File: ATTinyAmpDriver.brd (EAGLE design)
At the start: 30 x 15 mm, 31 parts, among them Q1 SI2301CDS, Q2 BC846, U1 SPX5205M5-L-3-3, U2 ATTINY5-TSHR, U3 MCP6L2-X_SN, X1 DIODES, X2 INPUT

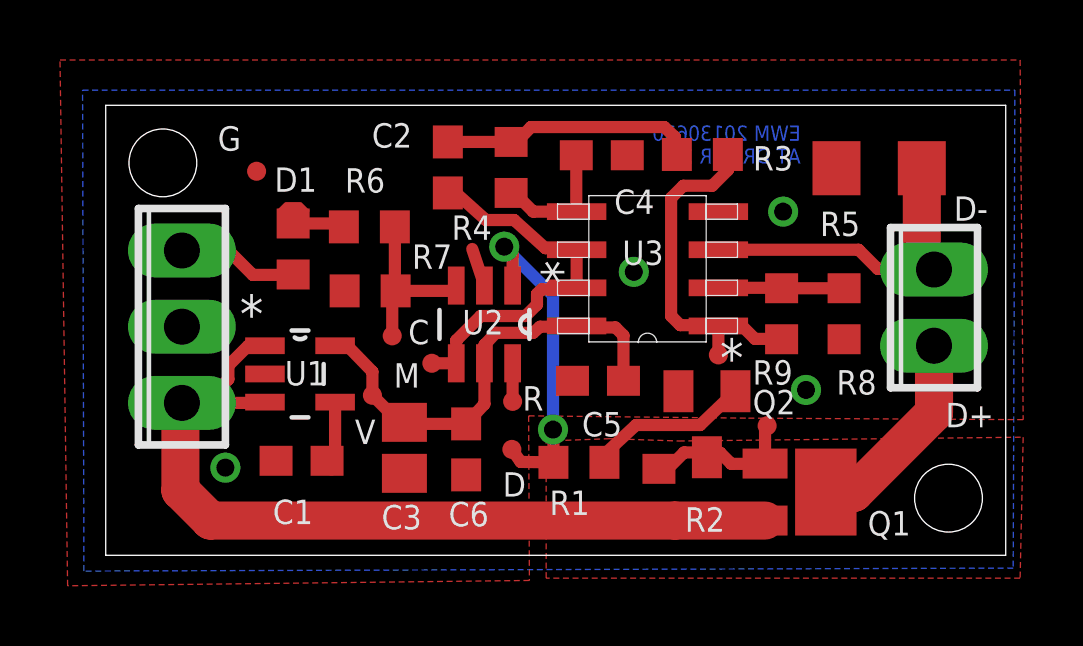
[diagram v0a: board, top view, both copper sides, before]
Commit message: Changed C3 to 1206 47uF
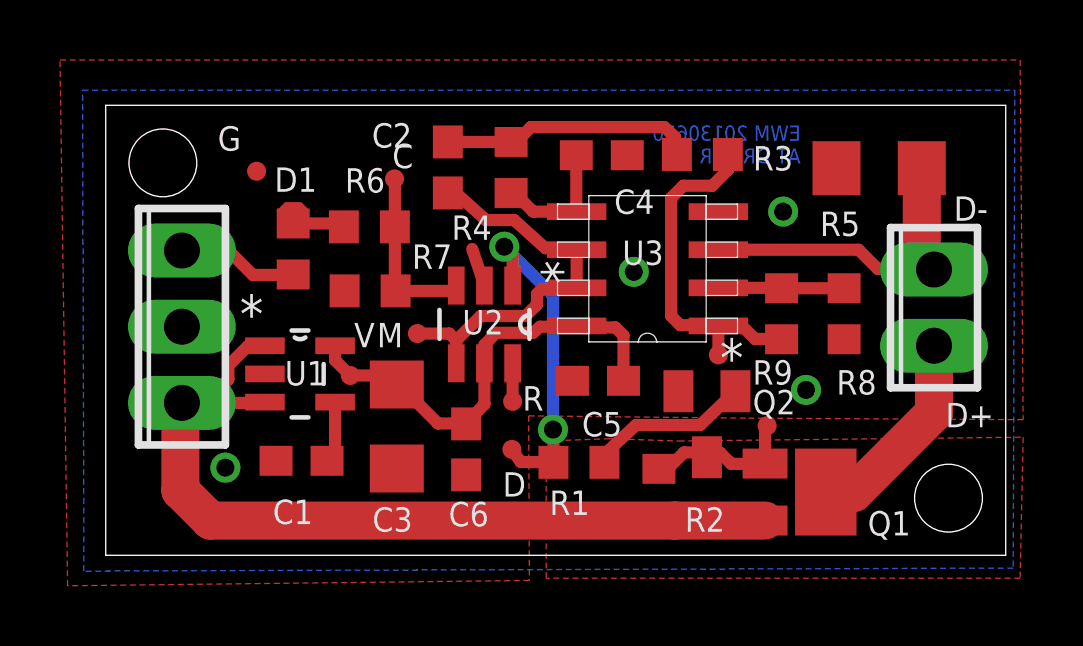
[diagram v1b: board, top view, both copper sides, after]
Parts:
- C3: value 10u -> 47u; device resistor:C0805 -> resistor:C1206
- moved TPICLK 5.23 mm to (9.63, 12.5)
- moved MEASURE 1.10 mm to (10.4, 7.39)
- moved +5V 0.99 mm to (8.15, 5.99)
- moved C3 0.76 mm to (9.70, 4.29)
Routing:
- net MEASURE: track 12.8 -> 13.4 mm
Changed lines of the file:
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@@
 AT DRIVER 3</text>
 <text x="13.2334" y="1.9558" size="0.8128" layer="25">D</text>
-<text x="10.0838" y="7.0358" size="0.8128" layer="25">C</text>
+<text x="9.5504" y="12.9032" size="0.8128" layer="25">C</text>
 <text x="3.7338" y="13.4874" size="0.8128" layer="25">G</text>
 <text x="13.8938" y="4.826" size="0.8128" layer="25">R</text>
-<text x="8.3058" y="3.7084" size="0.8128" layer="25">V</text>
+<text x="8.2804" y="6.9342" size="0.8128" layer="25">V</text>
 <dimension x1="0" y1="15" x2="0" y2="0" x3="-1.9812" y3="7.5" textsize="1.778" layer="20" unit="inch" precision="3"/>
 <dimension x1="0" y1="0" x2="30" y2="0" x3="15" y3="-3.5052" textsize="1.778" layer="20" unit="inch" precision="3"/>
-<text x="9.6012" y="5.588" size="0.8128" layer="25">M</text>
+<text x="9.0424" y="6.9342" size="0.8128" layer="25">M</text>
 </plain>
 <attributes>
@@
 <attribute name="VALUE" x="5.588" y="3.556" size="1.27" layer="27" rot="R90"/>
 </element>
-<element name="C3" library="resistor" package="C0805" value="10u" x="9.9568" y="3.5814" smashed="yes" rot="R270">
-<attribute name="NAME" x="9.1948" y="0.8636" size="0.8128" layer="25"/>
-<attribute name="VALUE" x="7.6708" y="4.4704" size="1.27" layer="27" rot="R270"/>
-<attribute name="DIGIKEY" value="445-7534-1-ND" x="9.9568" y="3.5814" size="1.778" layer="27" rot="R270" display="off"/>
-<attribute name="DIGIKEY_COST" value=".10" x="9.9568" y="3.5814" size="1.778" layer="27" rot="R270" display="off"/>
+<element name="C3" library="resistor" package="C1206" value="47u" x="9.7028" y="4.2926" smashed="yes" rot="R270">
+<attribute name="NAME" x="8.89" y="0.7874" size="0.8128" layer="25"/>
+<attribute name="VALUE" x="7.4168" y="5.1816" size="1.27" layer="27" rot="R270"/>
+<attribute name="DIGIKEY" value="399-5508-1-ND" x="9.7028" y="4.2926" size="1.778" layer="27" rot="R270" display="off"/>
+<attribute name="DIGIKEY_COST" value=".67" x="9.7028" y="4.2926" size="1.778" layer="27" rot="R270" display="off"/>
 </element>
 <element name="R5" library="resistor" package="R1206" value=".1" x="25.781" y="12.9032" smashed="yes">
@@
 </element>
 <element name="TPIDATA" library="Personal" package="TPI_PAD" value="TPI" x="13.5382" y="3.5306"/>
-<element name="TPICLK" library="Personal" package="TPI_PAD" value="TPI" x="9.5504" y="7.3152"/>
-<element name="+5V" library="Personal" package="TPI_PAD" value="TPI" x="8.89" y="5.334"/>
+<element name="TPICLK" library="Personal" package="TPI_PAD" value="TPI" x="9.6266" y="12.5476"/>
+<element name="+5V" library="Personal" package="TPI_PAD" value="TPI" x="8.1534" y="5.9944"/>
 <element name="GND" library="Personal" package="TPI_PAD" value="TPI" x="5.0292" y="12.8016"/>
 <element name="C1" library="resistor" package="C0603" value="10n" x="6.5278" y="3.1496" smashed="yes" rot="R180">
@@
 </element>
 <element name="PWM" library="Personal" package="TPI_PAD" value="TPI" x="22.0472" y="4.318"/>
-<element name="MEASURE" library="Personal" package="TPI_PAD" value="TPI" x="10.8712" y="6.4008"/>
+<element name="MEASURE" library="Personal" package="TPI_PAD" value="TPI" x="10.3886" y="7.3914"/>
 <element name="OUTA" library="Personal" package="TPI_PAD" value="TPI" x="20.4216" y="6.6802"/>
 </elements>
@@
 <contactref element="U2" pad="5"/>
 <contactref element="+5V" pad="P$1"/>
-<wire x1="7.6454" y1="6.985" x2="8.0518" y2="6.985" width="0.4064" layer="1"/>
-<wire x1="8.0518" y1="6.985" x2="8.89" y2="6.1214" width="0.4064" layer="1"/>
-<wire x1="8.89" y1="5.334" x2="8.89" y2="6.1214" width="0.4064" layer="1"/>
-<wire x1="8.89" y1="5.334" x2="8.9662" y2="5.2832" width="0.4064" layer="1"/>
-<wire x1="8.9662" y1="5.2832" x2="8.9916" y2="5.2832" width="0.4064" layer="1"/>
-<wire x1="8.9916" y1="5.2832" x2="8.9916" y2="5.2578" width="0.4064" layer="1"/>
-<wire x1="9.9568" y1="4.4314" x2="9.7926" y2="4.4314" width="0.4064" layer="1"/>
-<wire x1="9.7926" y1="4.4314" x2="8.89" y2="5.334" width="0.4064" layer="1"/>
 <contactref element="C6" pad="1"/>
 <contactref element="C5" pad="1"/>
@@
 <wire x1="12.6238" y1="6.4008" x2="12.6238" y2="5.041" width="0.4064" layer="1"/>
 <wire x1="12.6238" y1="5.041" x2="12.0142" y2="4.3806" width="0.4064" layer="1"/>
-<wire x1="12.0142" y1="4.3806" x2="10.0076" y2="4.3806" width="0.4064" layer="1"/>
-<wire x1="10.0076" y1="4.3806" x2="9.9568" y2="4.4314" width="0.4064" layer="1"/>
+<wire x1="7.6454" y1="6.985" x2="7.6454" y2="6.5024" width="0.4064" layer="1"/>
+<wire x1="7.6454" y1="6.5024" x2="8.1534" y2="5.9944" width="0.4064" layer="1"/>
+<wire x1="8.1534" y1="5.9944" x2="9.401" y2="5.9944" width="0.4064" layer="1"/>
+<wire x1="9.401" y1="5.9944" x2="9.7028" y2="5.6926" width="0.4064" layer="1"/>
+<wire x1="9.7028" y1="5.6926" x2="9.776" y2="5.6926" width="0.4064" layer="1"/>
+<wire x1="9.776" y1="5.6926" x2="11.0744" y2="4.3942" width="0.4064" layer="1"/>
+<wire x1="11.0744" y1="4.3942" x2="12.0006" y2="4.3942" width="0.4064" layer="1"/>
+<wire x1="12.0006" y1="4.3942" x2="12.0142" y2="4.3806" width="0.4064" layer="1"/>
 </signal>
 <signal name="D-">
@@
 <wire x1="15.6464" y1="10.2362" x2="15.6972" y2="10.1854" width="0.4064" layer="1"/>
 <contactref element="MEASURE" pad="P$1"/>
-<wire x1="10.8712" y1="6.4008" x2="11.684" y2="6.4008" width="0.4064" layer="1"/>
+<wire x1="10.3886" y1="7.3914" x2="11.4554" y2="7.3914" width="0.4064" layer="1"/>
+<wire x1="11.4554" y1="7.3914" x2="11.684" y2="7.1628" width="0.4064" layer="1"/>
 </signal>
 <signal name="MOSFET">
@@
 <wire x1="9.6384" y1="8.8392" x2="9.6638" y2="8.8138" width="0.4064" layer="1"/>
 <wire x1="11.7094" y1="8.8138" x2="11.684" y2="8.9916" width="0.4064" layer="1"/>
-<wire x1="9.6638" y1="8.8138" x2="9.5504" y2="8.8138" width="0.4064" layer="1"/>
-<wire x1="9.5504" y1="8.8138" x2="9.5504" y2="7.3152" width="0.4064" layer="1"/>
 <wire x1="9.6638" y1="8.8138" x2="11.684" y2="8.8138" width="0.4064" layer="1"/>
 <wire x1="11.684" y1="8.8138" x2="11.684" y2="8.9916" width="0.4064" layer="1"/>
+<wire x1="9.6266" y1="12.5476" x2="9.6384" y2="12.5476" width="0.4064" layer="1"/>
+<wire x1="9.6384" y1="12.5476" x2="9.6384" y2="10.9474" width="0.4064" layer="1"/>
 </signal>
 <signal name="N$3">
@@
 </signal>
 </signals>
-<errors>
-</errors>
 </board>
 </drawing>

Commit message: Created Programming Fixture
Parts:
- +5V, GND, MEASURE, OUTA, PWM, RESET, TPICLK, TPIDATA: device Personal:TPI_PAD -> Combined:TPI_PAD
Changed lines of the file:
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@@
 <grid distance="0.001" unitdist="inch" unit="inch" style="lines" multiple="1" display="no" altdistance="0.025" altunitdist="inch" altunit="inch"/>
 <layers>
-<layer number="1" name="Top" color="4" fill="1" visible="yes" active="yes"/>
-<layer number="16" name="Bottom" color="1" fill="1" visible="yes" active="yes"/>
-<layer number="17" name="Pads" color="2" fill="1" visible="yes" active="yes"/>
-<layer number="18" name="Vias" color="2" fill="1" visible="yes" active="yes"/>
-<layer number="19" name="Unrouted" color="6" fill="1" visible="yes" active="yes"/>
+<layer number="1" name="Top" color="4" fill="1" visible="no" active="yes"/>
+<layer number="16" name="Bottom" color="1" fill="1" visible="no" active="yes"/>
+<layer number="17" name="Pads" color="2" fill="1" visible="no" active="yes"/>
+<layer number="18" name="Vias" color="2" fill="1" visible="no" active="yes"/>
+<layer number="19" name="Unrouted" color="6" fill="1" visible="no" active="yes"/>
 <layer number="20" name="Dimension" color="15" fill="1" visible="yes" active="yes"/>
-<layer number="21" name="tPlace" color="7" fill="1" visible="yes" active="yes"/>
-<layer number="22" name="bPlace" color="7" fill="1" visible="yes" active="yes"/>
-<layer number="23" name="tOrigins" color="15" fill="1" visible="yes" active="yes"/>
-<layer number="24" name="bOrigins" color="15" fill="1" visible="yes" active="yes"/>
-<layer number="25" name="tNames" color="7" fill="1" visible="yes" active="yes"/>
-<layer number="26" name="bNames" color="7" fill="1" visible="yes" active="yes"/>
+<layer number="21" name="tPlace" color="7" fill="1" visible="no" active="yes"/>
+<layer number="22" name="bPlace" color="7" fill="1" visible="no" active="yes"/>
+<layer number="23" name="tOrigins" color="15" fill="1" visible="no" active="yes"/>
+<layer number="24" name="bOrigins" color="15" fill="1" visible="no" active="yes"/>
+<layer number="25" name="tNames" color="7" fill="1" visible="no" active="yes"/>
+<layer number="26" name="bNames" color="7" fill="1" visible="no" active="yes"/>
 <layer number="27" name="tValues" color="7" fill="1" visible="no" active="yes"/>
 <layer number="28" name="bValues" color="7" fill="1" visible="no" active="yes"/>
@@
 <layer number="37" name="tTest" color="7" fill="1" visible="no" active="yes"/>
 <layer number="38" name="bTest" color="7" fill="1" visible="no" active="yes"/>
-<layer number="39" name="tKeepout" color="4" fill="11" visible="yes" active="yes"/>
-<layer number="40" name="bKeepout" color="1" fill="11" visible="yes" active="yes"/>
-<layer number="41" name="tRestrict" color="4" fill="10" visible="yes" active="yes"/>
-<layer number="42" name="bRestrict" color="1" fill="10" visible="yes" active="yes"/>
-<layer number="43" name="vRestrict" color="2" fill="10" visible="yes" active="yes"/>
+<layer number="39" name="tKeepout" color="4" fill="11" visible="no" active="yes"/>
+<layer number="40" name="bKeepout" color="1" fill="11" visible="no" active="yes"/>
+<layer number="41" name="tRestrict" color="4" fill="10" visible="no" active="yes"/>
+<layer number="42" name="bRestrict" color="1" fill="10" visible="no" active="yes"/>
+<layer number="43" name="vRestrict" color="2" fill="10" visible="no" active="yes"/>
 <layer number="44" name="Drills" color="7" fill="1" visible="no" active="yes"/>
-<layer number="45" name="Holes" color="7" fill="1" visible="yes" active="yes"/>
+<layer number="45" name="Holes" color="7" fill="1" visible="no" active="yes"/>
 <layer number="46" name="Milling" color="3" fill="1" visible="no" active="yes"/>
-<layer number="47" name="Measures" color="7" fill="1" visible="yes" active="yes"/>
+<layer number="47" name="Measures" color="7" fill="1" visible="no" active="yes"/>
 <layer number="48" name="Document" color="7" fill="1" visible="no" active="yes"/>
 <layer number="49" name="Reference" color="7" fill="1" visible="no" active="yes"/>
-<layer number="51" name="tDocu" color="7" fill="1" visible="yes" active="yes"/>
-<layer number="52" name="bDocu" color="7" fill="1" visible="yes" active="yes"/>
+<layer number="51" name="tDocu" color="7" fill="1" visible="no" active="yes"/>
+<layer number="52" name="bDocu" color="7" fill="1" visible="no" active="yes"/>
 <layer number="91" name="Nets" color="2" fill="1" visible="no" active="no"/>
 <layer number="92" name="Busses" color="1" fill="1" visible="no" active="no"/>
@@
 <layer number="97" name="Info" color="7" fill="1" visible="no" active="no"/>
 <layer number="98" name="Guide" color="6" fill="1" visible="no" active="no"/>
+<layer number="100" name="TestPads" color="7" fill="1" visible="yes" active="yes"/>
 <layer number="250" name="Descript" color="3" fill="1" visible="no" active="no"/>
 <layer number="251" name="SMDround" color="12" fill="11" visible="no" active="no"/>
@@
 <text x="8.2804" y="6.9342" size="0.8128" layer="25">V</text>
 <text x="9.0424" y="6.9342" size="0.8128" layer="25">M</text>
+<dimension x1="0" y1="0" x2="30" y2="0" x3="15" y3="-5.1562" textsize="1.778" layer="20" unit="inch" precision="3"/>
+<dimension x1="0" y1="15" x2="0" y2="0" x3="-4.699" y3="7.5" textsize="1.778" layer="20" unit="inch" precision="3"/>
 </plain>
 <attributes>
@@
 <attribute name="DIGIKEY_COST" value=".04" x="18.4404" y="2.032" size="1.778" layer="27" rot="R90" display="off"/>
 </element>
-<element name="TPIDATA" library="Personal" package="TPI_PAD" value="TPI" x="13.5382" y="3.5306"/>
-<element name="TPICLK" library="Personal" package="TPI_PAD" value="TPI" x="9.6266" y="12.5476"/>
-<element name="+5V" library="Personal" package="TPI_PAD" value="TPI" x="8.1534" y="5.9944"/>
-<element name="GND" library="Personal" package="TPI_PAD" value="TPI" x="5.0292" y="12.8016"/>
+<element name="TPIDATA" library="Combined" package="TPI_PAD" value="TPI" x="13.5382" y="3.5306"/>
+<element name="TPICLK" library="Combined" package="TPI_PAD" value="TPI" x="9.6266" y="12.5476"/>
+<element name="+5V" library="Combined" package="TPI_PAD" value="TPI" x="8.1534" y="5.9944"/>
+<element name="GND" library="Combined" package="TPI_PAD" value="TPI" x="5.0292" y="12.8016"/>
 <element name="C1" library="resistor" package="C0603" value="10n" x="6.5278" y="3.1496" smashed="yes" rot="R180">
 <attribute name="NAME" x="6.9088" y="1.8542" size="0.8128" layer="25" rot="R180"/>
@@
 <attribute name="DIGIKEY_COST" value=".10" x="6.5278" y="3.1496" size="1.778" layer="27" rot="R180" display="off"/>
 </element>
-<element name="RESET" library="Personal" package="TPI_PAD" value="TPI" x="13.5636" y="5.1308"/>
+<element name="RESET" library="Combined" package="TPI_PAD" value="TPI" x="13.5636" y="5.1308"/>
 <element name="R9" library="resistor" package="R0603" value="28.7K" x="22.5298" y="8.0518" smashed="yes" rot="R90">
 <attribute name="DIGIKEY" value="RMCF0603FT28R7CT-ND" x="22.5298" y="8.0518" size="1.778" layer="27" rot="R90" display="off"/>
@@
 <attribute name="VALUE" x="22.5806" y="8.9408" size="1.27" layer="27" rot="R270"/>
 </element>
-<element name="PWM" library="Personal" package="TPI_PAD" value="TPI" x="22.0472" y="4.318"/>
-<element name="MEASURE" library="Personal" package="TPI_PAD" value="TPI" x="10.3886" y="7.3914"/>
-<element name="OUTA" library="Personal" package="TPI_PAD" value="TPI" x="20.4216" y="6.6802"/>
+<element name="PWM" library="Combined" package="TPI_PAD" value="TPI" x="22.0472" y="4.318"/>
+<element name="MEASURE" library="Combined" package="TPI_PAD" value="TPI" x="10.3886" y="7.3914"/>
+<element name="OUTA" library="Combined" package="TPI_PAD" value="TPI" x="20.4216" y="6.6802"/>
 </elements>
 <signals>
